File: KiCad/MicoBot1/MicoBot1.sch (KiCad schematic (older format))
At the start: 21 parts, among them J1 +5v, J2 Bat, J3 Motor2, J4 Motor1, J5 GND, J6 ANALOG, J7 DIGITAL, J8 Serial, SW1 Rst, SW2 On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

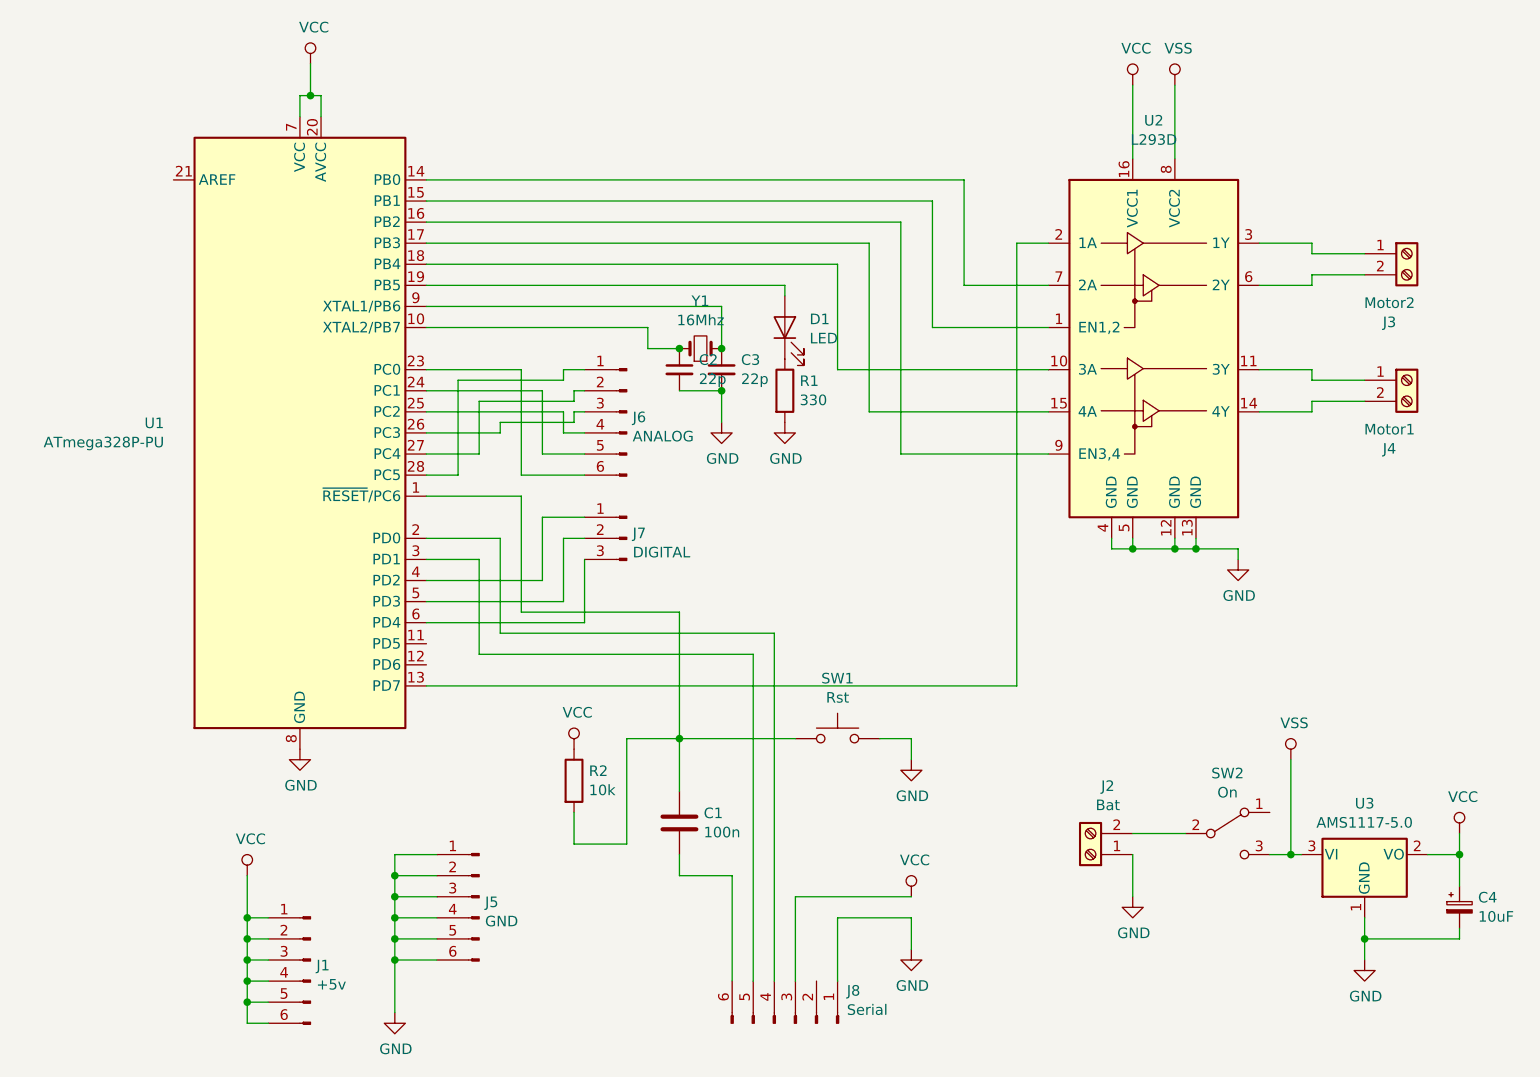
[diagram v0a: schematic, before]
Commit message: 
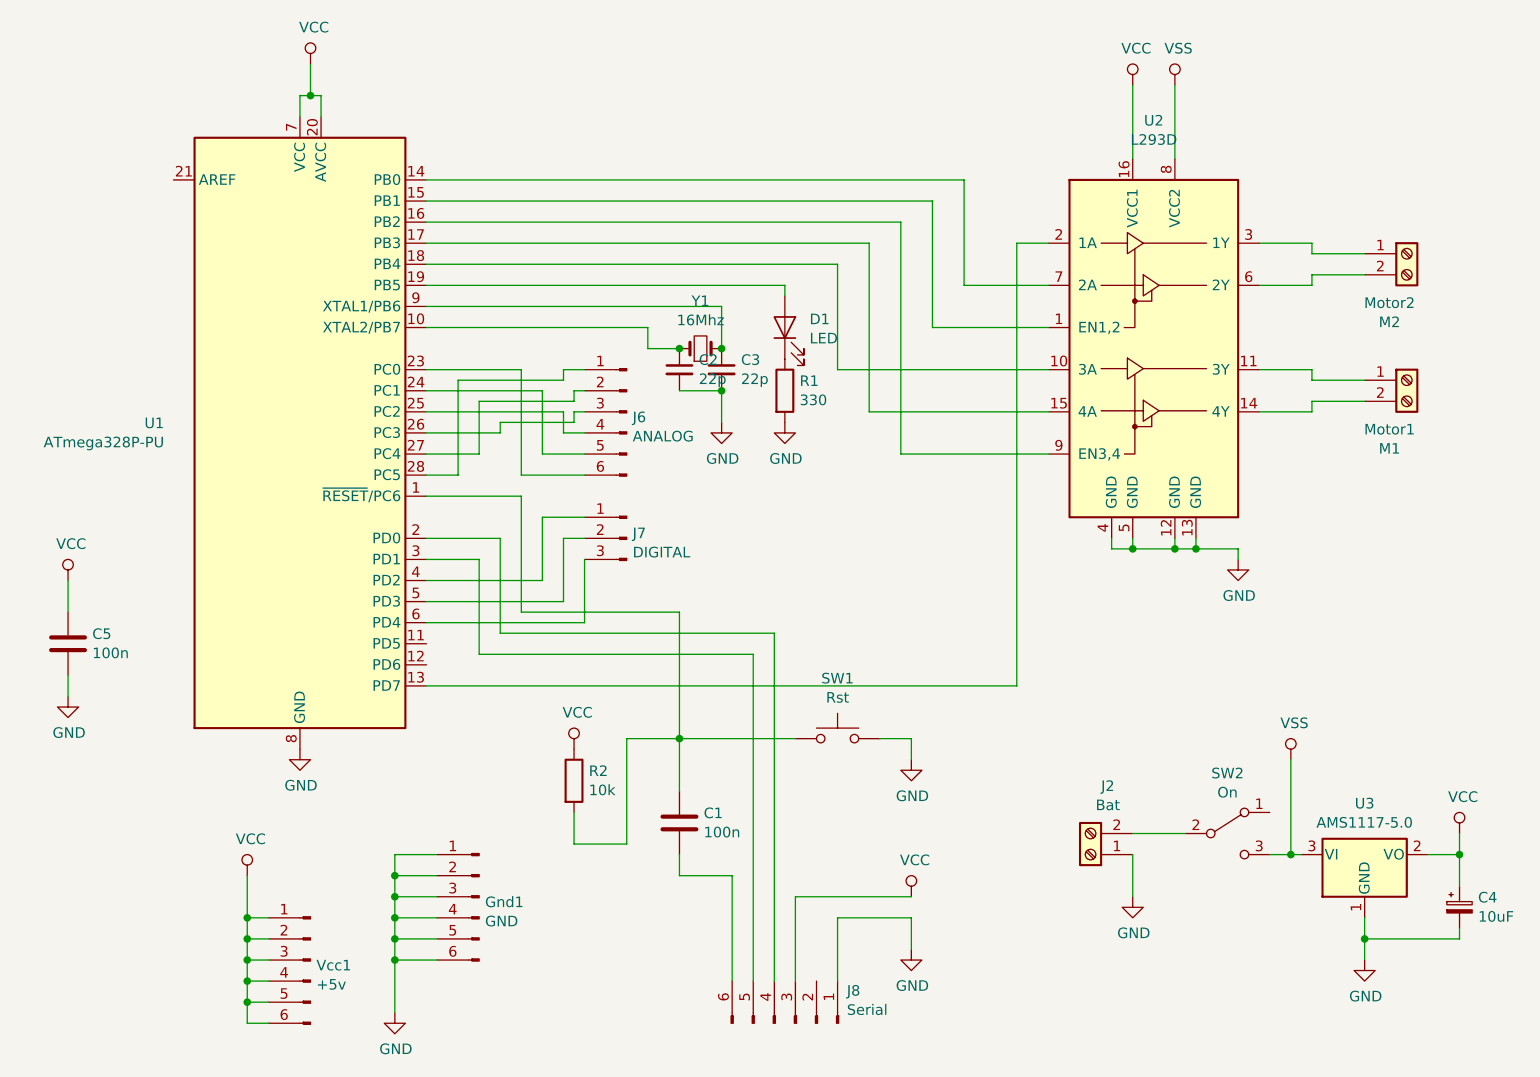
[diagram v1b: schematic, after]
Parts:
- added C5: 100n, Capacitor_SMD:C_1206_3216Metric, symbol Device:C
- renumbered J5 to Gnd1, J4 to M1, J3 to M2, J1 to Vcc1
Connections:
- net GND: now also C5.2
- net VCC: now also C5.1
